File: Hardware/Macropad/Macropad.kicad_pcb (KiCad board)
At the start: 2 copper layers, 3.4 x 3 mm, 172 parts, among them J1 USB_C_Receptacle_USB2.0, J2 Conn_01x04_Female, J3 Conn_02x03_Odd_Even, J4 USB_C_Receptacle_USB2.0, J5 USB_C_Receptacle_USB2.0, J6 USB_C_Receptacle_USB2.0, SW1 K40_1U, SW10 K01_1U, SW11 K42_1U, SW12 K32_1U, SW13 K22_1U, SW14 K12_1U, SW15 K02_1U, SW16 K43_1U, SW17 K33_1U, SW18 K23_1U, SW19 K13_1U, SW2 K30_1U, SW20 K03_1U, SW21 Rotary_Encoder_Switch, SW22 SW_Push, SW3 K20_1U, SW4 K10_1U, SW5 K00_1U, SW6 K41_1U, SW7 K31_1U, SW8 K21_1U, SW9 K11_1U, U1 TCR2EF33, U2 SRV05-4, U3 TPS2044D, U4 TUSB2046b, U5 ATmega32U4-AU, U6 SRV05-4, U7 SRV05-4, U8 SRV05-4, X1 KC2016K, X2 625L3C006M00000

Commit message: First pass of the layout done
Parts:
- removed C16, C30: 100nF, Capacitor_smd:C_0603_1608Metric
- removed D23: UG_LED_0, custom_footprint_library:SK6812-MINI-E
- removed D29: UG_LED_1, custom_footprint_library:SK6812-MINI-E
- removed FB3: Ferrite_Bead, Inductor_SMD:L_0805_2012Metric
- removed R12: OPT, resistor_smd:R_0603_1608Metric
- removed R17, R30: 4K7, resistor_smd:R_0603_1608Metric
- removed U3: TPS2044D, Package_SO:SOIC-16_3.9x9.9mm_P1.27mm
- added C40: 100nF, Capacitor_smd:C_0603_1608Metric, B.Cu at (60.8, 182.6)
- added C41: 100nF, Capacitor_smd:C_0603_1608Metric, B.Cu at (117.8, 182.4)
- added C42: 100nF, Capacitor_smd:C_0603_1608Metric, B.Cu at (79.7, 182.5)
- added C43: 100nF, Capacitor_smd:C_0603_1608Metric, B.Cu at (98.5, 182.5)
- added C44: 1uF, Capacitor_smd:C_0603_1608Metric, B.Cu at (68.9, 76.6)
- added C45: 1uF, Capacitor_smd:C_0603_1608Metric, F.Cu at (94.4, 62.7)
- added C46: 1uF, Capacitor_smd:C_0603_1608Metric, F.Cu at (122.3, 62.6)
- C10, C11, C13, C15, C17, C19, C20, C22, C24, C26, C27, C29, C32, C33, C34, C35, C36, C5, C6, C7, C9, D10, D11, D12, D13, D14, D15, D16, D17, D18, D19, D2, D20, D21, D22, D24, D3, D30, D35, D36, D4, D41, D42, D47, D48, D49, D5, D50, D6, D7, D8, D9, FB1, J1, J3, L1, R10, R11, R15, R18, R19, R22, R23, R24, R25, R26, R27, R28, R29, R3, R4, R5, R6, R7, R8, R9, SW22, U4, U6, U7, U8, X1, X2: moved to B.Cu
- C37, C39: value 100uF -> 1uF; footprint Capacitor_smd:C_1210_3225Metric -> Capacitor_smd:C_0603_1608Metric
- C38: value 100uF -> 100nF; footprint Capacitor_smd:C_1210_3225Metric -> Capacitor_smd:C_0603_1608Metric
- R1: value 1K -> 4K7; moved to B.Cu
- moved TP3 221.0 mm to (46.9, 78.7)
- moved TP1 219.2 mm to (50.5, 78.7)
- moved TP2 205.9 mm to (65.9, 69.7)
- moved R4 203.6 mm to (46.2, 74.3)
- moved C2 202.7 mm to (46.0, 66.7), turned to 180 degrees
- moved R3 200.2 mm to (51.5, 61.7), turned to 180 degrees
- moved C10 200.1 mm to (54.5, 161.3), turned to 270 degrees
- moved C1 198.9 mm to (46.0, 68.4), turned to 180 degrees
- moved L1 198.2 mm to (54.5, 67.5), turned to 270 degrees
- moved R6 194.3 mm to (54.5, 69.5), turned to 180 degrees
- moved R5 193.8 mm to (54.5, 65.5), turned to 180 degrees
- moved R10 193.0 mm to (68.9, 75.0)
- moved FB1 191.8 mm to (49.3, 74.9), turned to 90 degrees
- moved C3 189.4 mm to (54.5, 73.3), turned to 180 degrees
- moved FB2 189.4 mm to (54.2, 71.5), turned to 180 degrees
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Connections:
- net /USB_HUB/DM3n renamed /USB_HUB/D3-
- net /USB_HUB/DM4n renamed /USB_HUB/D4-
- net /USB_HUB/DP1p renamed /USB_HUB/D1+
- net /USB_HUB/DP2p renamed /USB_HUB/D2+
- net /USB_HUB/DP3n renamed /USB_HUB/D3+
- net /USB_HUB/DP4p renamed /USB_HUB/D4+
- C37 pad 1: VBUS1 -> +3V3
- C38 pad 1: VBUS2 -> +3V3
- C39 pad 1: VBUS3 -> +5V
- D35 pad 4: Net-(D29-Pad2) -> Net-(D35-Pad4)
- J4 pad A4: VBUS1 -> +5V
- J4 pad A6: DP2_P -> USB_D1+
- J4 pad A7: DM2_N -> USB_D1-
- J4 pad A9: VBUS1 -> +5V
- J4 pad B4: VBUS1 -> +5V
- J4 pad B6: DP2_P -> USB_D1+
- J4 pad B7: DM2_N -> USB_D1-
- J4 pad B9: VBUS1 -> +5V
- J5 pad A4: VBUS2 -> +5V
- J5 pad A6: DP3_P -> USB_D2+
- J5 pad A7: DM3_N -> USB_D2-
- J5 pad A9: VBUS2 -> +5V
- J5 pad B4: VBUS2 -> +5V
- J5 pad B6: DP3_P -> USB_D2+
- J5 pad B7: DM3_N -> USB_D2-
- J5 pad B9: VBUS2 -> +5V
- J6 pad A4: VBUS3 -> +5V
- J6 pad A6: DP4_P -> USB_D3+
- J6 pad A7: DM4_N -> USB_D3-
- J6 pad A9: VBUS3 -> +5V
- J6 pad B4: VBUS3 -> +5V
- J6 pad B6: DP4_P -> USB_D3+
- J6 pad B7: DM4_N -> USB_D3-
- J6 pad B9: VBUS3 -> +5V
- L1 pad 1: /USB/D+ -> /USB/D-
- L1 pad 2: /USB/D- -> /USB/D+
- L1 pad 3: Net-(J1-PadA7) -> Net-(J1-PadA6)
- L1 pad 4: Net-(J1-PadA6) -> Net-(J1-PadA7)
- R1 pad 1: Net-(R1-Pad1) -> Net-(C44-Pad2)
- R1 pad 2: +5V -> +3V3
- R16 pad 2: Net-(D23-Pad4) -> Net-(D35-Pad4)
- R22 pad 1: DP1_P -> USB_D1+
- R23 pad 1: DM1_N -> USB_D1-
- R23 pad 2: /USB_HUB/DM1n -> /USB_HUB/D1-
- R24 pad 1: DP2_P -> USB_D2+
- R25 pad 1: DM2_N -> USB_D2-
- R25 pad 2: /USB_HUB/DM1n -> /USB_HUB/D2-
- R26 pad 1: DP3_P -> USB_D3+
- R27 pad 1: DM3_N -> USB_D3-
- R28 pad 1: DP4_P -> USB_D4+
- R29 pad 1: DM4_N -> USB_D4-
- R5 pad 1: /USB/D+ -> /USB/D-
- R5 pad 2: Net-(J1-PadA6) -> Net-(J1-PadA7)
- R6 pad 1: /USB/D- -> /USB/D+
- R6 pad 2: Net-(J1-PadA7) -> Net-(J1-PadA6)
- R7 pad 1: USBD_P -> USB_D0-
- R7 pad 2: /USB/D+ -> /USB/D-
- R8 pad 1: USBD_N -> USB_D0+
- R8 pad 2: /USB/D- -> /USB/D+
- U1 pad 3: Net-(R1-Pad1) -> +5V
- U4 pad 1: USBD_P -> USB_D0+
- U4 pad 10: nOVRCUR1 -> +3V3
- U4 pad 11: /USB_HUB/DM1n -> /USB_HUB/D1-
- U4 pad 13: nPWRON2 -> Net-(U4-Pad13)
- U4 pad 14: nOVRCUR2 -> +3V3
- U4 pad 15: /USB_HUB/DM1n -> /USB_HUB/D2-
- U4 pad 17: nPWRON3 -> Net-(U4-Pad17)
- U4 pad 18: nOVRCUR3 -> +3V3
- U4 pad 2: USBD_N -> USB_D0-
- U4 pad 21: nPWRON4 -> Net-(U4-Pad21)
- U4 pad 22: nOVRCUR4 -> +3V3
- U4 pad 4: Net-(U4-Pad4) -> Net-(C44-Pad2)
- U4 pad 9: nPWRON1 -> Net-(U4-Pad9)
- U5 pad 1: COL[0] -> SCL
- U5 pad 12: Net-(U5-Pad12) -> COL[1]
- U5 pad 18: RGB_OUT -> COL[2]
- U5 pad 19: SDA -> ROW[4]
- U5 pad 20: SCL -> ROW[3]
- U5 pad 21: Net-(U5-Pad21) -> ROW[2]
- U5 pad 22: Net-(U5-Pad22) -> ROW[1]
- U5 pad 25: Net-(U5-Pad25) -> ROW[0]
- U5 pad 27: COL[3] -> ROW[5]
- U5 pad 28: Net-(U5-Pad28) -> COL[3]
- U5 pad 29: ROT_ENC_A -> Net-(U5-Pad29)
- U5 pad 3: DM1_N -> USB_D4-
- U5 pad 30: ROT_ENC_B -> Net-(U5-Pad30)
- U5 pad 31: ROW[4] -> ROT_ENC_A
- U5 pad 32: ROW[5] -> ROT_ENC_B
- U5 pad 36: ROW[3] -> Net-(U5-Pad36)
- U5 pad 37: ROW[2] -> Net-(U5-Pad37)
- U5 pad 38: ROW[1] -> Net-(U5-Pad38)
- U5 pad 39: ROW[0] -> Net-(U5-Pad39)
- U5 pad 4: DP1_P -> USB_D4+
- U5 pad 40: COL[1] -> RGB_OUT
- U5 pad 41: COL[2] -> SDA
- U5 pad 8: Net-(U5-Pad8) -> COL[0]
- U6 pad 1: DP2_P -> Net-(U6-Pad1)
- U6 pad 3: DM2_N -> USB_D1+
- U6 pad 4: Net-(U6-Pad4) -> USB_D1-
- U6 pad 5: VBUS1 -> +5V
- U7 pad 1: DP3_P -> Net-(U7-Pad1)
- U7 pad 3: DM3_N -> USB_D2+
- U7 pad 4: Net-(U7-Pad4) -> USB_D2-
- U7 pad 5: VBUS2 -> +5V
- U8 pad 1: DP4_P -> Net-(U8-Pad1)
- U8 pad 3: DM4_N -> USB_D3+
- U8 pad 4: Net-(U8-Pad4) -> USB_D3-
- U8 pad 5: VBUS3 -> +5V
- X1 pad 1: Net-(R17-Pad1) -> +3V3
- X2 pad 1: Net-(R30-Pad2) -> +3V3
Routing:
- net ROW[0]: track 0.00 -> 158.1 mm, vias 0 -> 8
- net ROW[1]: track 0.00 -> 136.9 mm, vias 0 -> 7
- net ROW[2]: track 0.00 -> 117.3 mm, vias 0 -> 7
- net COL[0]: track 0.00 -> 117.1 mm, vias 0 -> 9
- net ROW[3]: track 0.00 -> 98.8 mm, vias 0 -> 7
- net COL[1]: track 0.00 -> 93.7 mm, vias 0 -> 5
- net +5V: track 0.00 -> 87.8 mm, vias 0 -> 20
- net COL[2]: track 0.00 -> 86.5 mm, vias 0 -> 5
- net ROW[4]: track 0.00 -> 78.8 mm, vias 0 -> 7
- net COL[3]: track 0.00 -> 77.5 mm, vias 0 -> 5
- net GND: track 0.00 -> 56.3 mm, vias 0 -> 40
- net SDA: track 0.00 -> 48.0 mm, vias 0 -> 2
- net SCL: track 0.00 -> 44.9 mm, vias 0 -> 2
- net USB_D3+: track 0.00 -> 44.0 mm
- net USB_D3-: track 0.00 -> 41.6 mm, vias 0 -> 1
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- added copper zone on F.Cu, net +3V3
- added copper zone on F.Cu, net +5V
- added copper zone on B.Cu, net GND
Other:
- board size 3.4 x 3 mm -> 88.9 x 135.9 mm

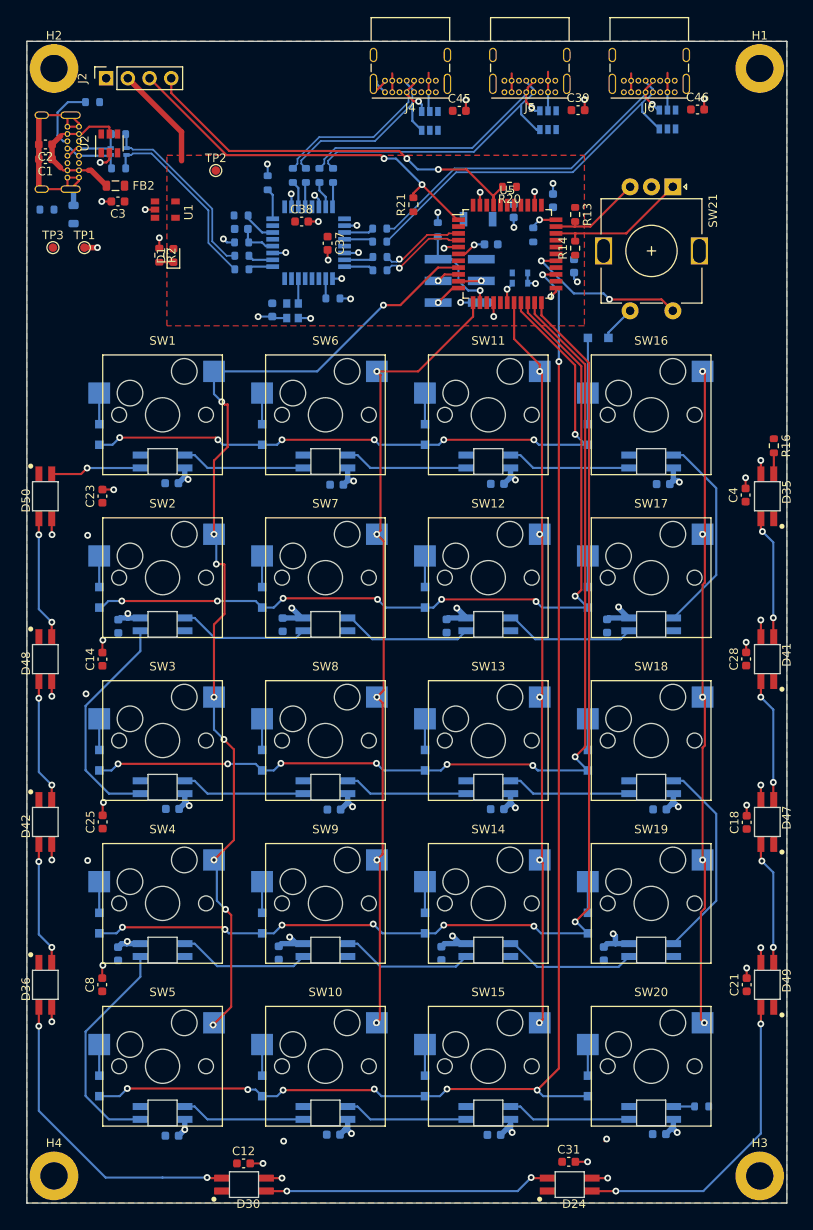
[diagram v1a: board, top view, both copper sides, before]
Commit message: Redoing layout with key switches upside down for better LED placement
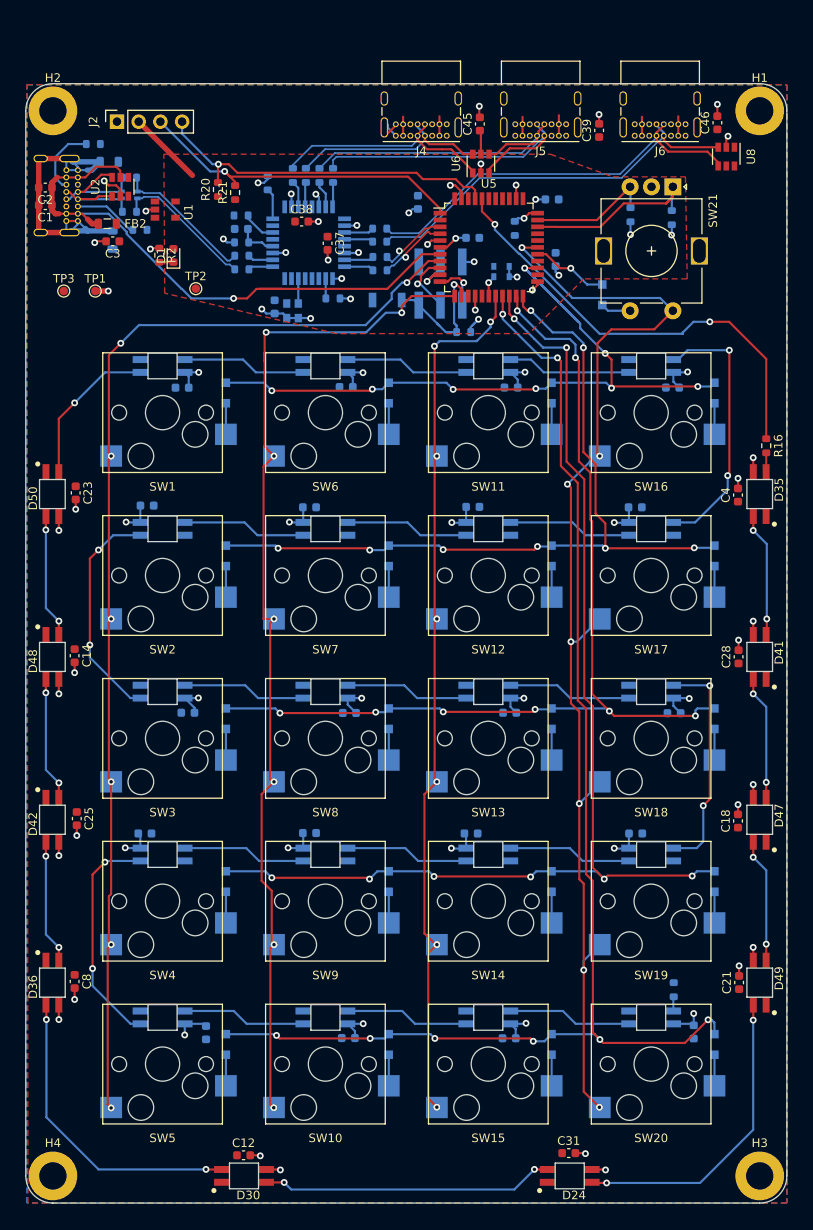
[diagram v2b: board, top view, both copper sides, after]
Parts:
- removed U7: SRV05-4, Package_TO_SOT_SMD:SOT-23-6
- added FB3: Ferrite_Bead, Inductor_SMD:L_0805_2012Metric, B.Cu at (53.5, 68.7)
- R13, R14: moved to B.Cu
- U6, U8: moved to F.Cu
- moved R20 34.1 mm to (66.2, 71.9), turned to 90 degrees
- moved R21 20.9 mm to (68.2, 72.3)
- moved D5 16.5 mm to (67.1, 151.7), turned to 270 degrees
- moved D10 16.5 mm to (86.1, 151.7), turned to 270 degrees
- moved D15 16.5 mm to (105.2, 151.7), turned to 270 degrees
- moved D20 16.5 mm to (124.2, 151.7), turned to 270 degrees
- moved D2 16.5 mm to (67.1, 94.5), turned to 270 degrees
- moved D3 16.5 mm to (67.1, 113.6), turned to 270 degrees
- moved D12 16.5 mm to (105.2, 94.5), turned to 270 degrees
- moved D13 16.5 mm to (105.2, 113.6), turned to 270 degrees
- moved D17 16.5 mm to (124.2, 94.5), turned to 270 degrees
- moved D18 16.5 mm to (124.2, 113.6), turned to 270 degrees
- moved D4 16.5 mm to (67.1, 132.6), turned to 270 degrees
- moved D6 16.5 mm to (67.1, 170.7), turned to 270 degrees
- moved D7 16.5 mm to (86.1, 94.5), turned to 270 degrees
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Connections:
- D17 pad 2: ENCODER -> Net-(D17-Pad2)
- D22 pad 1: ENCODER -> ROW[5]
- SW16 pad 1: ENCODER -> Net-(D17-Pad2)
- SW21 pad S2: ROW[5] -> COL[3]
- U2 pad 1: Net-(J1-PadA7) -> Net-(J1-PadA6)
- U2 pad 3: Net-(J1-PadA6) -> Net-(U2-Pad3)
- U2 pad 6: Net-(U2-Pad6) -> Net-(J1-PadA7)
- U5 pad 19: ROW[4] -> ROW[0]
- U5 pad 20: ROW[3] -> ROW[1]
- U5 pad 22: ROW[1] -> ROW[3]
- U5 pad 25: ROW[0] -> ROW[4]
- U6 pad 1: Net-(U6-Pad1) -> USB_D1-
- U6 pad 3: USB_D1+ -> USB_D2+
- U6 pad 4: USB_D1- -> USB_D2-
- U6 pad 6: Net-(U6-Pad6) -> USB_D1+
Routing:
- net COL[3]: track 77.5 -> 137.6 mm, vias 5 -> 7
- net RGB_OUT: track 0.00 -> 52.9 mm, vias 0 -> 2
- net VBUS: track 17.7 -> 70.4 mm, vias 0 -> 1
- net COL[1]: track 93.7 -> 120.4 mm, vias 5 -> 7
- net COL[2]: track 86.5 -> 103.2 mm, vias 5 -> 7
- net COL[0]: track 117.1 -> 132.9 mm, vias 9 -> 7
- net Net-(C1-Pad2): track 27.0 -> 38.3 mm
- net ROW[5]: track 19.5 -> 9.06 mm, vias 2 -> 1
- net ENCODER: track 10.1 -> 0.00 mm
- net ROW[4]: track 78.8 -> 87.8 mm, vias 7 -> 8
- net Net-(J1-PadA5): track 0.00 -> 7.56 mm
- net Net-(D43-Pad4): track 23.9 -> 31.3 mm, vias 0 -> 2
- net RGB[1]: track 10.7 -> 18.0 mm
- net SDA: track 48.0 -> 41.6 mm, vias 2 -> 1
- net Net-(J1-PadA7): track 7.11 -> 13.5 mm
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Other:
- board size 88.9 x 135.9 mm -> 89 x 130.9 mm

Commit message: Layout done, cleaned up schematic and generated gerbers
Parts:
- added C16: 100nF, Capacitor_smd:C_0603_1608Metric, F.Cu at (62.2, 79.1)
- added C30: 1uF, Capacitor_smd:C_0603_1608Metric, F.Cu at (68.8, 75.0)
- SW22: footprint button_switch_smd:SW_SPST_B3U-1000P -> custom_footprint_library:SW_SPST_B3U-1000P
- moved C3 9.29 mm to (61.6, 72.9), turned to 90 degrees
- moved D1 6.86 mm to (67.4, 82.0)
- moved R2 6.86 mm to (65.8, 82.0)
- moved U1 4.26 mm to (62.5, 75.4)
- moved J2 2.60 mm to (54.9, 61.5)
- moved TP2 2.04 mm to (65.3, 84.6)
- moved U8 0.74 mm to (126.3, 68.3)
- moved SW22 0.43 mm to (85.5, 84.8)
- moved C32 0.41 mm to (72.4, 85.7)
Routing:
- net +5V: track 89.7 -> 114.7 mm, vias 20 -> 40
- net SCL: track 39.6 -> 44.8 mm
- net +3V3: track 41.3 -> 46.3 mm
- net GND: track 57.0 -> 59.7 mm, vias 37 -> 39
- net SDA: track 41.6 -> 43.9 mm
- net USB_D3+: track 46.8 -> 48.6 mm
- net USB_D3-: track 47.8 -> 48.5 mm
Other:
- board text added: "+5V"
- board text added: "GND"
- board text added: "MISO"
- board text added: "MOSI"
- board text added: "Macropad - v0 Alex Binos 2021"
- board text added: "RST"
- board text added: "SCK"
